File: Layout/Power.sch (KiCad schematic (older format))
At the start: 19 parts, among them U4 TPS562200, U5 AP2112K-3.3

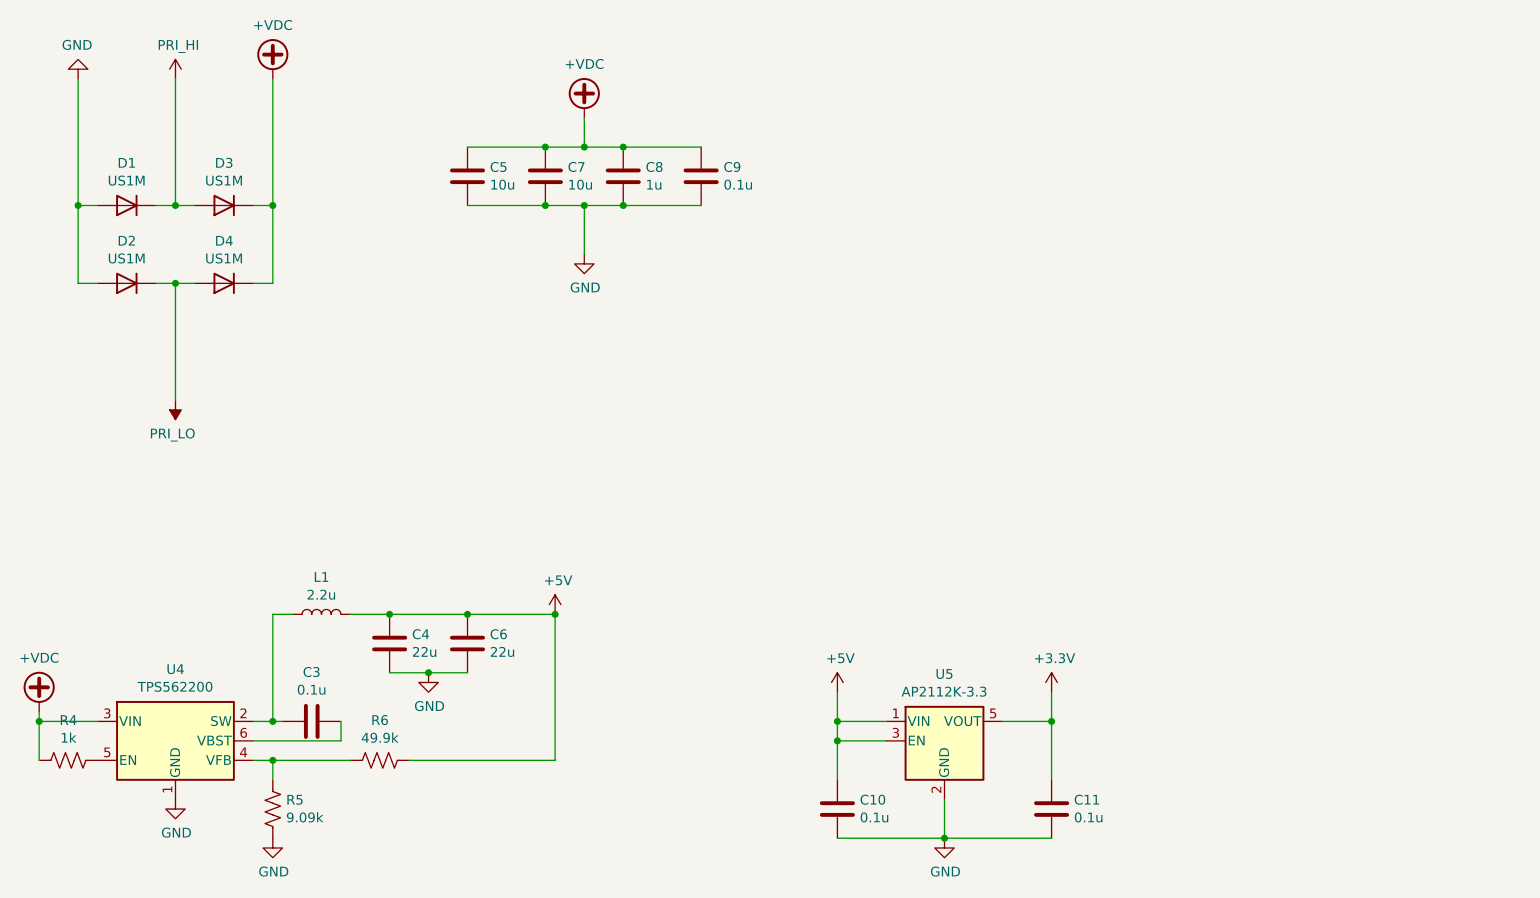
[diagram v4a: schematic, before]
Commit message: Update schematic for new processor
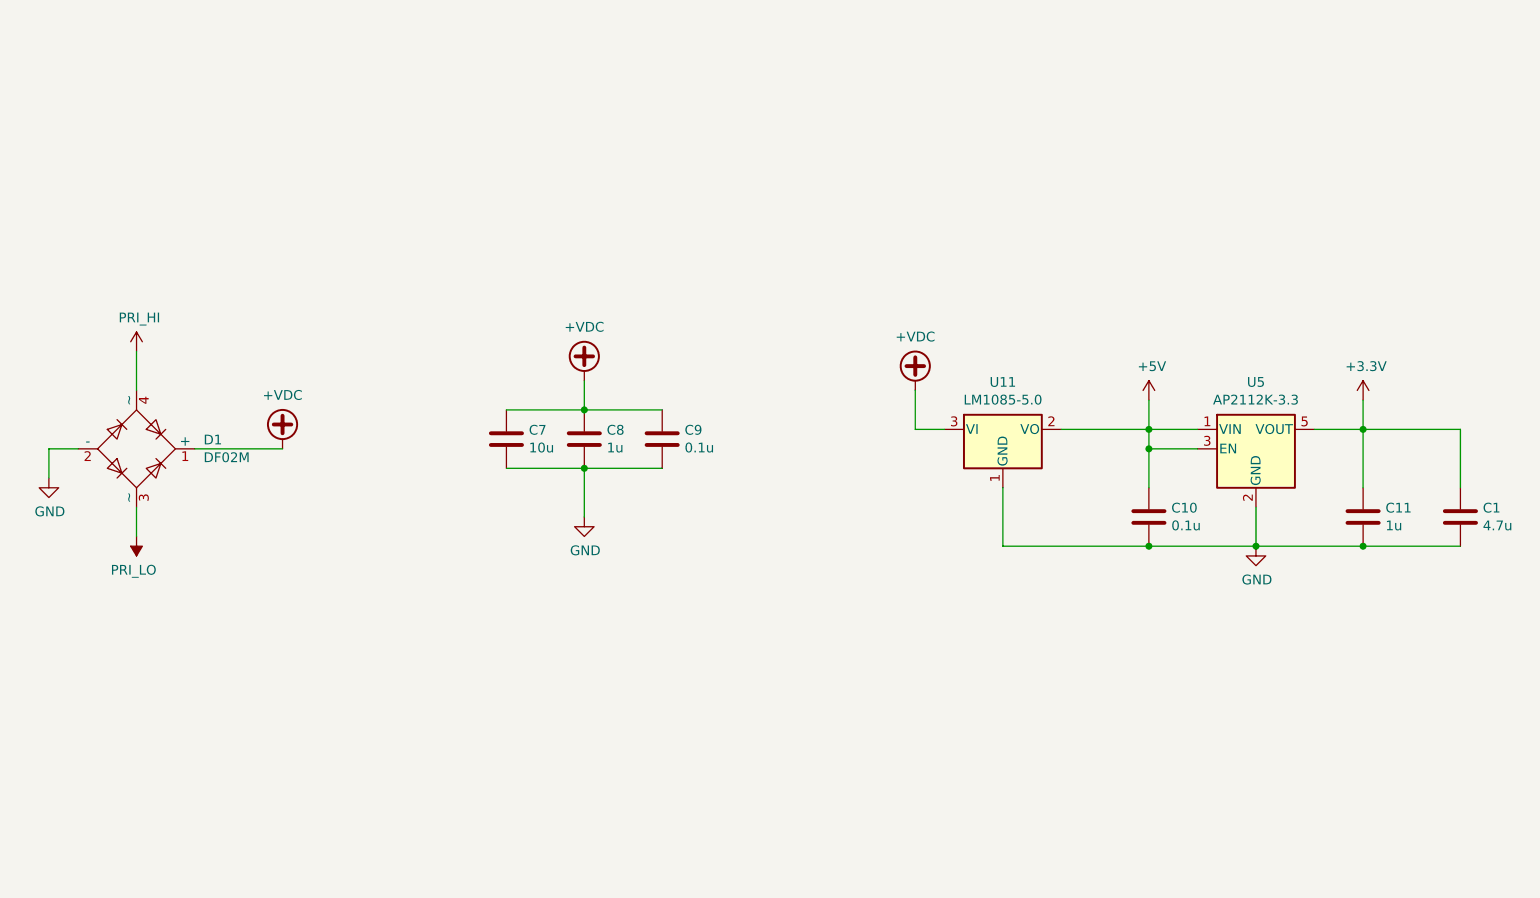
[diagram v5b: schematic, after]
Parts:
- removed C3: 0.1u, Capacitor_SMD:C_0603_1608Metric_Pad1.05x0.95mm_HandSolder, symbol Device:C
- removed C4, C6: 22u, Capacitor_SMD:C_0603_1608Metric_Pad1.05x0.95mm_HandSolder, symbol Device:C
- removed C5: 10u, Capacitor_SMD:C_0603_1608Metric_Pad1.05x0.95mm_HandSolder, symbol Device:C
- removed D1, D2, D3, D4: US1M, Diode_SMD:D_SMA, symbol Diode:US1M
- removed L1: 2.2u, Inductor_SMD:L_Taiyo-Yuden_NR-40xx_HandSoldering, symbol Device:L
- removed R4: 1k, Resistor_SMD:R_0603_1608Metric_Pad1.05x0.95mm_HandSolder, symbol Device:R_US
- removed R5: 9.09k, Resistor_SMD:R_0603_1608Metric_Pad1.05x0.95mm_HandSolder, symbol Device:R_US
- removed R6: 49.9k, Resistor_SMD:R_0603_1608Metric_Pad1.05x0.95mm_HandSolder, symbol Device:R_US
- removed U4: TPS562200, Package_TO_SOT_SMD:SOT-23-6, symbol Regulator_Switching:TPS562200
- added C1: 4.7u, Capacitor_SMD:C_0603_1608Metric_Pad1.05x0.95mm_HandSolder, symbol Device:C
- added D1: DF02M, Diode_THT:Diode_Bridge_DIP-4_W7.62mm_P5.08mm, symbol Diode_Bridge:DF02M
- added U11: LM1085-5.0, Package_TO_SOT_SMD:TO-263-3_TabPin2, symbol Regulator_Linear:LM1085-5.0
- C11: value 0.1u -> 1u
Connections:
- net +3V3: now also C1.1
- net +5V: now also U11.2 (VO)
- net +VDC: now also D1.1 (+), U11.3 (VI)
- net GND: now also C1.2, D1.2 (-), U11.1 (GND)
- net PRI_HI: now also D1.4 (~~)
- net PRI_LO: now also D1.3 (~~)
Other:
- moved on the sheet: C10, C11, C7, C8, C9, U5
